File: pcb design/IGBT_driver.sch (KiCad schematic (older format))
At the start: 26 parts, among them Q13 NPN, Q14 PNP, U1 ISO5852S

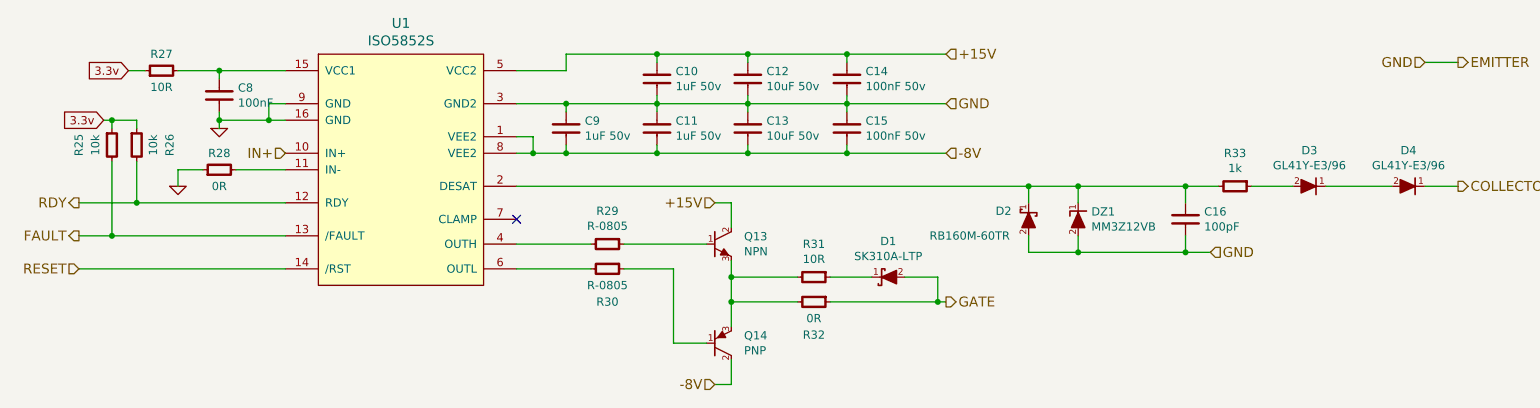
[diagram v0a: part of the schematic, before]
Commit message: Add footprints, more layout and graphics
Signed-off-by: Marcos Chaparro <mchaparro@paltatech.com>
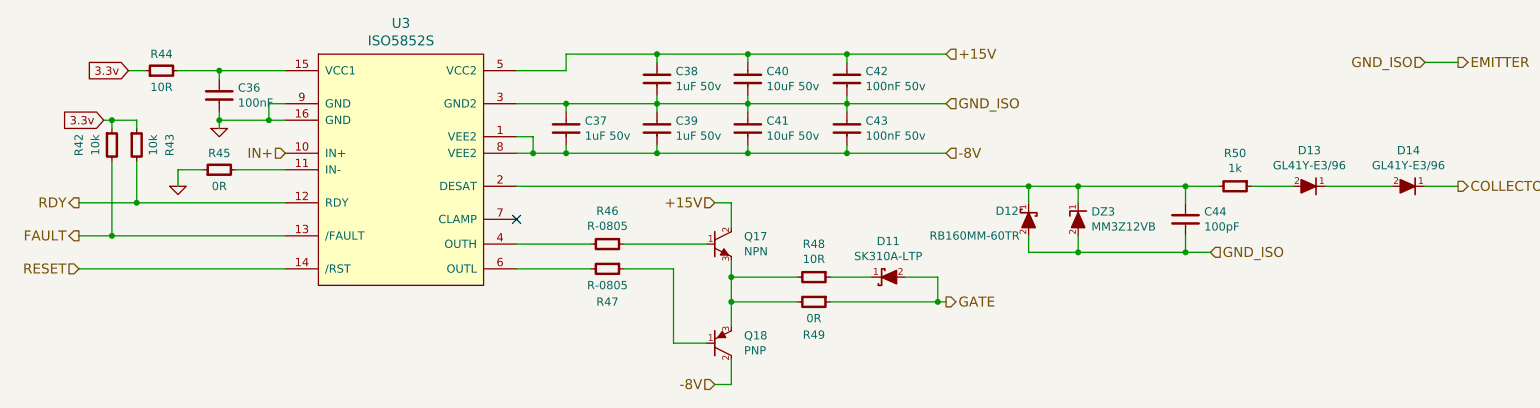
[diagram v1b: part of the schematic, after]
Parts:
- D1: footprint (none) -> w_smd_diode:do214ac
- D2: value RB160M-60TR -> RB160MM-60TR; footprint (none) -> paltatech:SOD-123F; mfg# RB160M-60TR -> RB160MM-60TR
- D3, D4: footprint (none) -> paltatech:melf-DO-213AB
- DZ1: footprint (none) -> smd-semi:SOD-323F
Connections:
- net GND: no longer C10.2, C11.1, C12.2, C13.1, C14.2, C15.1, C16.2, C9.1, D2.2 (A), DZ1.2 (A), U1.3 (GND2)
- new net EMITTER: C10.2, C11.1, C12.2, C13.1, C14.2, C15.1, C16.2, C9.1, D2.2 (A), DZ1.2 (A), U1.3 (GND2)
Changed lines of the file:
@@
 $Descr A4 11693 8268
 encoding utf-8
-Sheet 2 4
+Sheet 4 4
 Title ""
-Date ""
-Rev ""
-Comp ""
+Date "2016-11-09"
+Rev "A"
+Comp "PALTA TECH"
 Comment1 ""
 Comment2 ""
@@
 AR Path="/5822D62D/5822D80D" Ref="U1"  Part="1"
 AR Path="/5824556D/5822D80D" Ref="U3"  Part="1"
-F 0 "U1" H 3750 4837 60  0000 C CNN
+F 0 "U3" H 3750 4837 60  0000 C CNN
 F 1 "ISO5852S" H 3750 4731 60  0000 C CNN
 F 2 "Housings_SOIC:SOIC-16_7.5x10.3mm_Pitch1.27mm" H 3750 3850 60  0001 C CNN
@@
 AR Path="/5822D62D/5822D8A3" Ref="Q13"  Part="1"
 AR Path="/5824556D/5822D8A3" Ref="Q17"  Part="1"
-F 0 "Q13" H 5827 4446 50  0000 L CNN
+F 0 "Q17" H 5827 4446 50  0000 L CNN
 F 1 "NPN" H 5827 4355 50  0000 L CNN
 F 2 "SMD_Packages:DPAK-2" H 5700 4400 60  0001 C CNN
@@
 AR Path="/5822D62D/5822D994" Ref="Q14"  Part="1"
 AR Path="/5824556D/5822D994" Ref="Q18"  Part="1"
-F 0 "Q14" H 5827 5046 50  0000 L CNN
+F 0 "Q18" H 5827 5046 50  0000 L CNN
 F 1 "PNP" H 5827 4955 50  0000 L CNN
 F 2 "SMD_Packages:DPAK-2" H 5700 5000 60  0001 C CNN
@@
 AR Path="/5822D62D/5822DA10" Ref="D1"  Part="1"
 AR Path="/5824556D/5822DA10" Ref="D11"  Part="1"
-F 0 "D1" V 6483 4600 50  0000 C CNN
+F 0 "D11" V 6483 4600 50  0000 C CNN
 F 1 "SK310A-LTP" V 6574 4600 50  0000 C CNN
-F 2 "" H 6700 4600 60  0000 C CNN
+F 2 "w_smd_diode:do214ac" H 6700 4600 60  0001 C CNN
 F 3 "" H 6700 4600 60  0000 C CNN
 F 4 "SK310A-LTP" H 6700 4600 60  0001 C CNN "mfg#"
@@
 AR Path="/5822D62D/5822DB82" Ref="D2"  Part="1"
 AR Path="/5824556D/5822DB82" Ref="D12"  Part="1"
-F 0 "D2" H 7750 4200 50  0000 R CNN
-F 1 "RB160M-60TR" H 8150 4350 50  0000 R CNN
-F 2 "" H 7550 4250 60  0000 C CNN
+F 0 "D12" H 7750 4200 50  0000 R CNN
+F 1 "RB160MM-60TR" H 8150 4350 50  0000 R CNN
+F 2 "paltatech:SOD-123F" H 7550 4250 60  0001 C CNN
 F 3 "" H 7550 4250 60  0000 C CNN
-F 4 "RB160M-60TR" H 7550 4250 60  0001 C CNN "mfg#"
+F 4 "RB160MM-60TR" H 7550 4250 60  0001 C CNN "mfg#"
 	1    7550 4250
 	-1   0    0    1
@@
 AR Path="/5822D62D/5822DBF0" Ref="DZ1"  Part="1"
 AR Path="/5824556D/5822DBF0" Ref="DZ3"  Part="1"
-F 0 "DZ1" H 7930 4296 50  0000 L CNN
+F 0 "DZ3" H 7930 4296 50  0000 L CNN
 F 1 "MM3Z12VB" H 7930 4205 50  0000 L CNN
-F 2 "" H 7850 4250 60  0000 C CNN
+F 2 "smd-semi:SOD-323F" H 7850 4250 60  0001 C CNN
 F 3 "" H 7850 4250 60  0000 C CNN
 F 4 "MM3Z12VB" H 7850 4250 60  0001 C CNN "mfg#"
@@
 AR Path="/5822D62D/5822DD15" Ref="D3"  Part="1"
 AR Path="/5824556D/5822DD15" Ref="D13"  Part="1"
-F 0 "D3" V 9467 4050 50  0000 C CNN
+F 0 "D13" V 9467 4050 50  0000 C CNN
 F 1 "GL41Y-E3/96" V 9376 4050 50  0000 C CNN
-F 2 "" H 9250 4050 60  0000 C CNN
+F 2 "paltatech:melf-DO-213AB" H 9250 4050 60  0001 C CNN
 F 3 "" H 9250 4050 60  0000 C CNN
 F 4 "GL41Y-E3/96" H 9250 4050 60  0001 C CNN "mfg#"
@@
 AR Path="/5822D62D/5822DDF3" Ref="D4"  Part="1"
 AR Path="/5824556D/5822DDF3" Ref="D14"  Part="1"
-F 0 "D4" V 10067 4050 50  0000 C CNN
+F 0 "D14" V 10067 4050 50  0000 C CNN
 F 1 "GL41Y-E3/96" V 9976 4050 50  0000 C CNN
-F 2 "" H 9850 4050 60  0000 C CNN
+F 2 "paltatech:melf-DO-213AB" H 9850 4050 60  0001 C CNN
 F 3 "" H 9850 4050 60  0000 C CNN
 F 4 "GL41Y-E3/96" H 9850 4050 60  0001 C CNN "mfg#"
@@
 AR Path="/5822D62D/58240348" Ref="C10"  Part="1"
 AR Path="/5824556D/58240348" Ref="C38"  Part="1"
-F 0 "C10" H 5413 3446 50  0000 L CNN
+F 0 "C38" H 5413 3446 50  0000 L CNN
 F 1 "1uF 50v" H 5413 3355 50  0000 L CNN
 F 2 "IPC7351-Nominal:CAPC2012X70" H 5300 3400 50  0001 C CNN
@@
 AR Path="/5822D62D/5824044E" Ref="C9"  Part="1"
 AR Path="/5824556D/5824044E" Ref="C37"  Part="1"
-F 0 "C9" H 4863 3746 50  0000 L CNN
+F 0 "C37" H 4863 3746 50  0000 L CNN
 F 1 "1uF 50v" H 4863 3655 50  0000 L CNN
 F 2 "IPC7351-Nominal:CAPC2012X70" H 4750 3700 50  0001 C CNN
@@
 AR Path="/5822D62D/58240493" Ref="C11"  Part="1"
 AR Path="/5824556D/58240493" Ref="C39"  Part="1"
-F 0 "C11" H 5413 3746 50  0000 L CNN
+F 0 "C39" H 5413 3746 50  0000 L CNN
 F 1 "1uF 50v" H 5413 3655 50  0000 L CNN
 F 2 "IPC7351-Nominal:CAPC2012X70" H 5300 3700 50  0001 C CNN
@@
 AR Path="/5822D62D/582406D3" Ref="C12"  Part="1"
 AR Path="/5824556D/582406D3" Ref="C40"  Part="1"
-F 0 "C12" H 5963 3446 50  0000 L CNN
+F 0 "C40" H 5963 3446 50  0000 L CNN
 F 1 "10uF 50v" H 5963 3355 50  0000 L CNN
 F 2 "IPC7351-Nominal:CAPC3216X70" H 5850 3400 50  0001 C CNN
@@
 AR Path="/5822D62D/58240848" Ref="C13"  Part="1"
 AR Path="/5824556D/58240848" Ref="C41"  Part="1"
-F 0 "C13" H 5963 3746 50  0000 L CNN
+F 0 "C41" H 5963 3746 50  0000 L CNN
 F 1 "10uF 50v" H 5963 3655 50  0000 L CNN
 F 2 "IPC7351-Nominal:CAPC3216X70" H 5850 3700 50  0001 C CNN
@@
 AR Path="/5822D62D/582408B6" Ref="C14"  Part="1"
 AR Path="/5824556D/582408B6" Ref="C42"  Part="1"
-F 0 "C14" H 6563 3446 50  0000 L CNN
+F 0 "C42" H 6563 3446 50  0000 L CNN
 F 1 "100nF 50v" H 6563 3355 50  0000 L CNN
 F 2 "IPC7351-Nominal:CAPC2012X70" H 6450 3400 50  0001 C CNN
@@
 AR Path="/5822D62D/58240925" Ref="C15"  Part="1"
 AR Path="/5824556D/58240925" Ref="C43"  Part="1"
-F 0 "C15" H 6563 3746 50  0000 L CNN
+F 0 "C43" H 6563 3746 50  0000 L CNN
 F 1 "100nF 50v" H 6563 3655 50  0000 L CNN
 F 2 "IPC7351-Nominal:CAPC2012X70" H 6450 3700 50  0001 C CNN
@@
 Connection ~ 5850 3850
 Text HLabel 7050 3550 2    60   Input ~ 0
-GND
+GND_ISO
 Text HLabel 7050 3250 2    60   Input ~ 0
 +15V
@@
 AR Path="/5822D62D/5824153A" Ref="R28"  Part="1"
 AR Path="/5824556D/5824153A" Ref="R45"  Part="1"
-F 0 "R28" V 2750 3950 50  0000 C CNN
+F 0 "R45" V 2750 3950 50  0000 C CNN
 F 1 "0R" V 2550 3950 50  0000 C CNN
 F 2 "IPC7351-Nominal:RESC1608X50" H 2650 3950 50  0001 C CNN
@@
 P 2400 4050
 AR Path="/5822D62D/582416B6" Ref="#PWR01"  Part="1"
-AR Path="/5824556D/582416B6" Ref="#PWR015"  Part="1"
-F 0 "#PWR015" H 2400 4050 30  0001 C CNN
+AR Path="/5824556D/582416B6" Ref="#PWR014"  Part="1"
+F 0 "#PWR014" H 2400 4050 30  0001 C CNN
 F 1 "GND" H 2400 3980 30  0001 C CNN
 F 2 "" H 2400 4050 60  0000 C CNN
@@
 P 2650 3700
 AR Path="/5822D62D/58241AEC" Ref="#PWR02"  Part="1"
-AR Path="/5824556D/58241AEC" Ref="#PWR016"  Part="1"
-F 0 "#PWR016" H 2650 3700 30  0001 C CNN
+AR Path="/5824556D/58241AEC" Ref="#PWR015"  Part="1"
+F 0 "#PWR015" H 2650 3700 30  0001 C CNN
 F 1 "GND" H 2650 3630 30  0001 C CNN
 F 2 "" H 2650 3700 60  0000 C CNN
@@
 AR Path="/5822D62D/582417BD" Ref="C8"  Part="1"
 AR Path="/5824556D/582417BD" Ref="C36"  Part="1"
-F 0 "C8" H 2763 3546 50  0000 L CNN
+F 0 "C36" H 2763 3546 50  0000 L CNN
 F 1 "100nF" H 2763 3455 50  0000 L CNN
 F 2 "IPC7351-Nominal:CAPC1608X55" H 2650 3500 50  0001 C CNN
@@
 AR Path="/5822D62D/58241F2C" Ref="R27"  Part="1"
 AR Path="/5824556D/58241F2C" Ref="R44"  Part="1"
-F 0 "R27" V 2400 3350 50  0000 C CNN
+F 0 "R44" V 2400 3350 50  0000 C CNN
 F 1 "10R" V 2200 3350 50  0000 C CNN
 F 2 "IPC7351-Nominal:RESC1608X50" H 2300 3350 50  0001 C CNN
@@
 AR Path="/5822D62D/58242366" Ref="R29"  Part="1"
 AR Path="/5824556D/58242366" Ref="R46"  Part="1"
-F 0 "R29" V 4800 4400 50  0000 C CNN
+F 0 "R46" V 4800 4400 50  0000 C CNN
 F 1 "R-0805" V 4891 4400 50  0000 C CNN
 F 2 "IPC7351-Nominal:RESC2012X50" H 5000 4400 50  0001 C CNN
@@
 AR Path="/5822D62D/5824246D" Ref="R30"  Part="1"
 AR Path="/5824556D/5824246D" Ref="R47"  Part="1"
-F 0 "R30" V 5200 4550 50  0000 C CNN
+F 0 "R47" V 5200 4550 50  0000 C CNN
 F 1 "R-0805" V 5100 4550 50  0000 C CNN
 F 2 "IPC7351-Nominal:RESC2012X50" H 5000 4550 50  0001 C CNN
@@
 AR Path="/5822D62D/5824286A" Ref="R31"  Part="1"
 AR Path="/5824556D/5824286A" Ref="R48"  Part="1"
-F 0 "R31" V 6050 4600 50  0000 C CNN
+F 0 "R48" V 6050 4600 50  0000 C CNN
 F 1 "10R" V 6141 4600 50  0000 C CNN
 F 2 "IPC7351-Nominal:RESC2012X50" H 6250 4600 50  0001 C CNN
@@
 AR Path="/5822D62D/58242871" Ref="R32"  Part="1"
 AR Path="/5824556D/58242871" Ref="R49"  Part="1"
-F 0 "R32" V 6450 4750 50  0000 C CNN
+F 0 "R49" V 6450 4750 50  0000 C CNN
 F 1 "0R" V 6350 4750 50  0000 C CNN
 F 2 "IPC7351-Nominal:RESC2012X50" H 6250 4750 50  0001 C CNN
@@
 AR Path="/5822D62D/58237039" Ref="R25"  Part="1"
 AR Path="/5824556D/58237039" Ref="R42"  Part="1"
-F 0 "R25" V 1800 3800 50  0000 C CNN
+F 0 "R42" V 1800 3800 50  0000 C CNN
 F 1 "10k" V 1900 3800 50  0000 C CNN
 F 2 "IPC7351-Nominal:RESC1608X50" H 2000 3800 50  0001 C CNN
@@
 AR Path="/5822D62D/582375EC" Ref="R26"  Part="1"
 AR Path="/5824556D/582375EC" Ref="R43"  Part="1"
-F 0 "R26" V 2350 3800 50  0000 C CNN
+F 0 "R43" V 2350 3800 50  0000 C CNN
 F 1 "10k" V 2250 3800 50  0000 C CNN
 F 2 "IPC7351-Nominal:RESC1608X50" H 2150 3800 50  0001 C CNN
@@
 AR Path="/5822D62D/5823827A" Ref="C16"  Part="1"
 AR Path="/5824556D/5823827A" Ref="C44"  Part="1"
-F 0 "C16" H 8613 4296 50  0000 L CNN
+F 0 "C44" H 8613 4296 50  0000 L CNN
 F 1 "100pF" H 8613 4205 50  0000 L CNN
 F 2 "IPC7351-Nominal:CAPC2012X70" H 8500 4250 50  0001 C CNN
@@
 AR Path="/5822D62D/582385C6" Ref="R33"  Part="1"
 AR Path="/5824556D/582385C6" Ref="R50"  Part="1"
-F 0 "R33" V 8600 4050 50  0000 C CNN
+F 0 "R50" V 8600 4050 50  0000 C CNN
 F 1 "1k" V 8691 4050 50  0000 C CNN
 F 2 "IPC7351-Nominal:RESC2012X50" H 8800 4050 50  0001 C CNN
@@
 Connection ~ 7850 4450
 Connection ~ 8500 4450
-Text HLabel 8650 4450 2    60   Input ~ 0
-GND
 Text HLabel 10150 4050 2    60   Output ~ 0
 COLLECTOR
@@
 Text HLabel 10150 3300 2    60   Output ~ 0
 EMITTER
-Text HLabel 9950 3300 0    60   Input ~ 0
-GND
 Wire Wire Line
 	9950 3300 10150 3300
@@
 Wire Wire Line
 	1800 4550 3050 4550
+Text HLabel 8650 4450 2    60   Input ~ 0
+GND_ISO
+Text HLabel 9950 3300 0    60   Input ~ 0
+GND_ISO
 $EndSCHEMATC

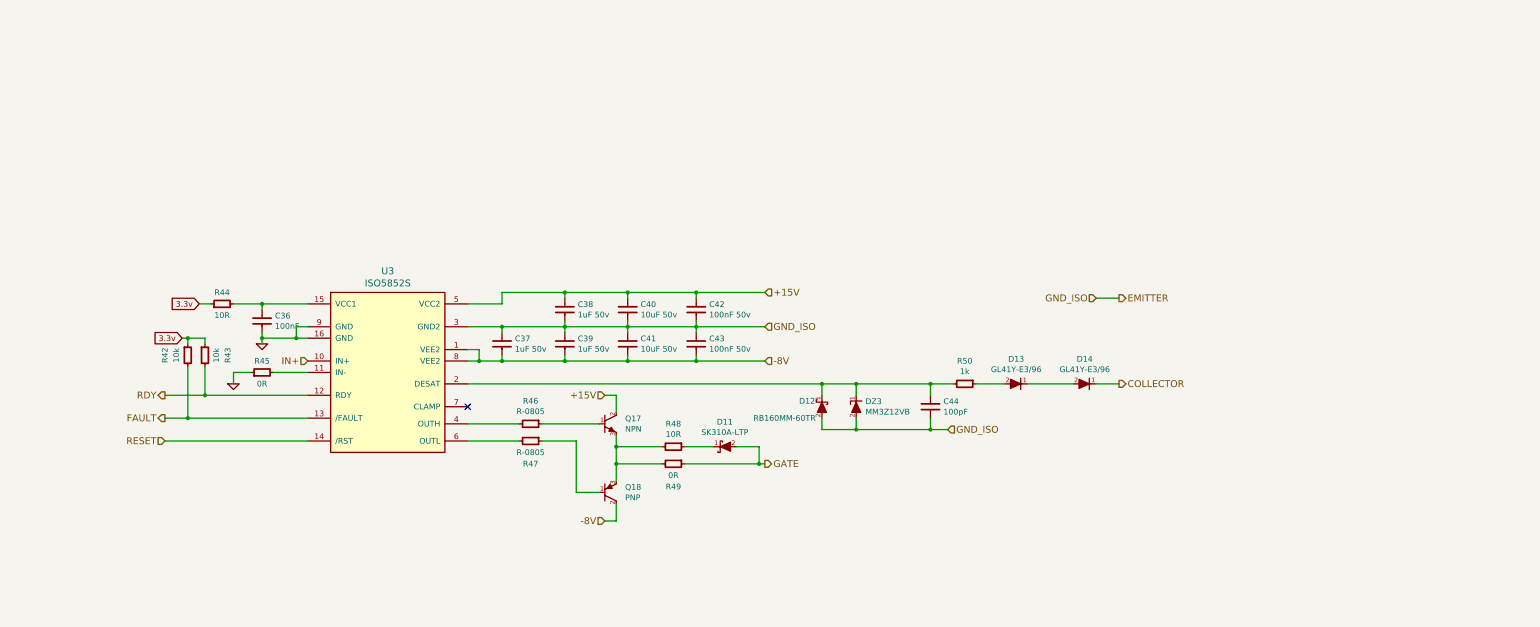
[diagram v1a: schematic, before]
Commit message: Larger gate resistors, added gate caps, added comments and images to the schematic
Signed-off-by: Marcos Chaparro <mchaparro@paltatech.com>
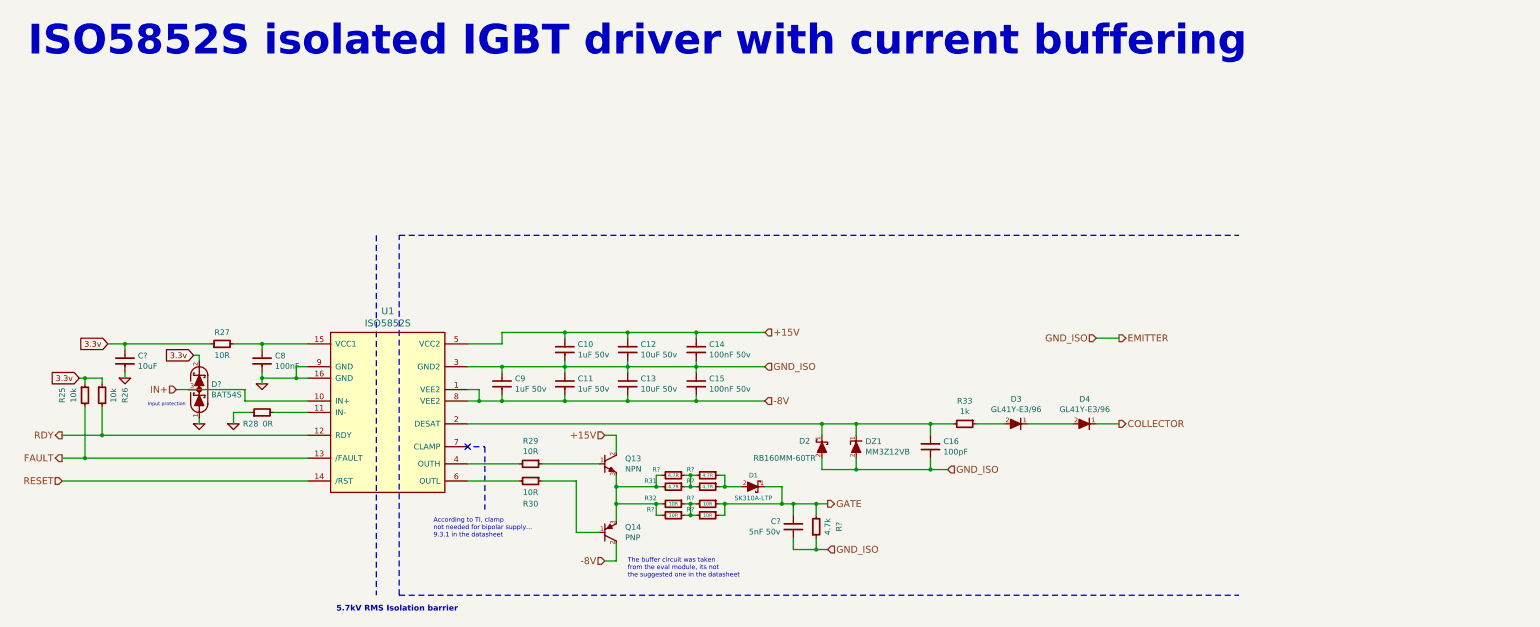
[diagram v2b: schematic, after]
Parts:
- added C?: 5nF 50v, IPC7351-Nominal:CAPC2012X70, symbol C-0805
- added C?: 10uF, IPC7351-Nominal:CAPC1608X55, symbol C-0603
- added D?: BAT54S, smd-semi:SOT-23, symbol BAT54S
- added R?: 4.7k, IPC7351-Nominal:RESC2012X50, symbol R-0805
- added R? (x3): 4.7R, IPC7351-Nominal:RESC3225X60, symbol R-0805
- added R? (x3): 10R, IPC7351-Nominal:RESC3225X60, symbol R-0805
- R29, R30: value R-0805 -> 10R
- R31: value 10R -> 4.7R; footprint IPC7351-Nominal:RESC2012X50 -> IPC7351-Nominal:RESC3225X60; BOM RES SMD 1k 5% [0805] -> RES SMD 1k 5% [2512]
- R32: value 0R -> 10R; footprint IPC7351-Nominal:RESC2012X50 -> IPC7351-Nominal:RESC3225X60; BOM RES SMD 1k 5% [0805] -> RES SMD 1k 5% [2512]
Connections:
- net 3.3v: now also C?.1, D?.2 (K)
- net EMITTER: now also C?.2, R?.1
- net GATE: now also D1.1 (K), C?.1, R?.1, R?.1, R?.2; no longer D1.2 (A), R32.1
- net GND: now also C?.2, D?.1 (A)
- net at Q13.3 (E), Q14.3 (E), R31.2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: now also R?.2, R?.2
- net at R31.1: now also R?.1, R?.2, R?.2; no longer D1.1 (K)
- new net: D1.2 (A), R?.1, R?.1
- new net: R32.1, R?.1, R?.2, R?.2
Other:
- note added: "5.7kV RMS Isolation barrier"
- note added: "According to TI, clamp\nnot needed for bipolar supply...\n9.3.1 in the datasheet"
- note added: "ISO5852S isolated IGBT driver with current buffering"
- note added: "Input protection"
- note added: "The buffer circuit was taken\nfrom the eval module, its not\nthe suggested one in the datasheet"
- moved on the sheet: C10, C11, C12, C13, C14, C15, C16, C8, C9, D1, D2, D3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

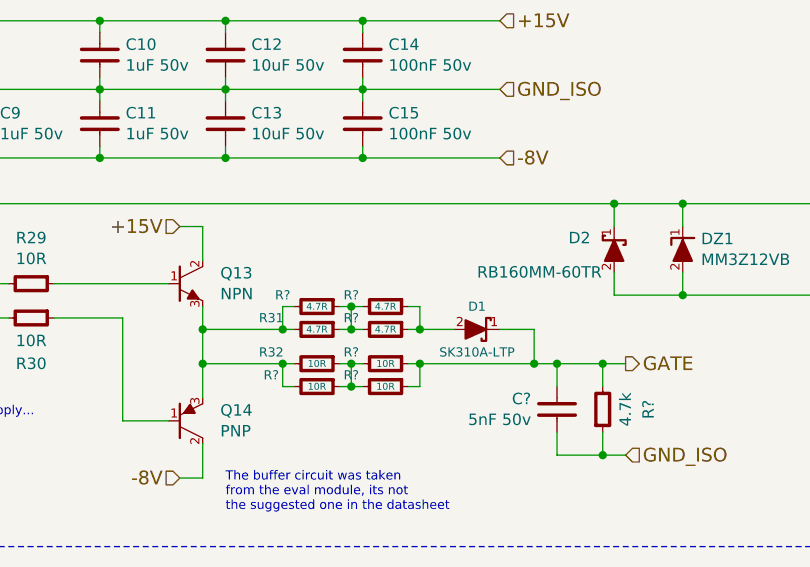
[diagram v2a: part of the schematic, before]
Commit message: Added schottky between gate and 15v supply
Signed-off-by: Marcos Chaparro <mchaparro@paltatech.com>
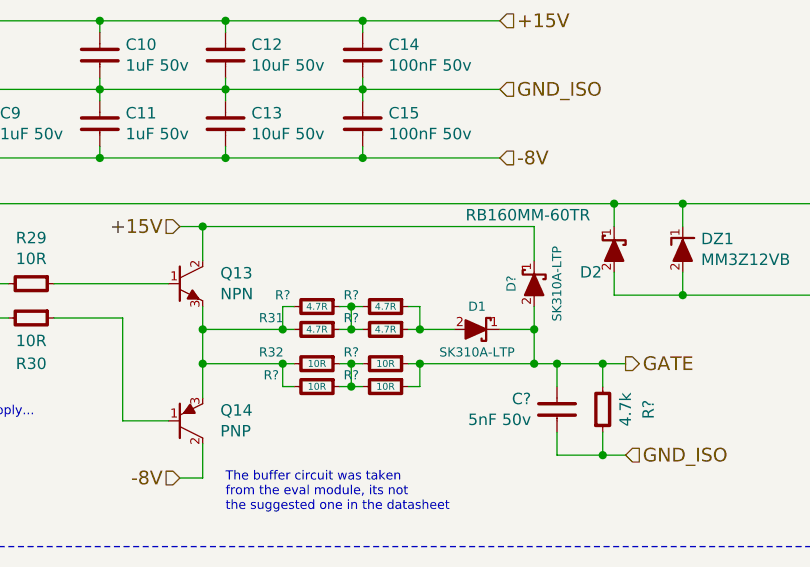
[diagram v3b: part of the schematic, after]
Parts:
- added D?: SK310A-LTP, w_smd_diode:do214ac, symbol SCHOTTKY
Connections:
- net +15V: now also D?.1 (K)
- net GATE: now also D?.2 (A)
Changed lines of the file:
@@
 AR Path="/5822D62D/5822DB82" Ref="D2"  Part="1"
 AR Path="/5824556D/5822DB82" Ref="D12"  Part="1"
-F 0 "D2" H 7750 4550 50  0000 R CNN
-F 1 "RB160MM-60TR" H 8150 4700 50  0000 R CNN
+F 0 "D2" H 7700 4700 50  0000 R CNN
+F 1 "RB160MM-60TR" H 8200 4450 50  0000 R CNN
 F 2 "paltatech:SOD-123F" H 7550 4600 60  0001 C CNN
 F 3 "" H 7550 4600 60  0000 C CNN
@@
 	6650 5100 7600 5100
 Wire Wire Line
-	7200 5100 7200 4950
+	7200 4850 7200 5100
 Wire Wire Line
 	7200 4950 7050 4950
@@
 	5750 4650 5750 4500
 Wire Wire Line
-	5750 4500 5650 4500
+	5650 4500 7200 4500
 Text HLabel 5650 5600 0    60   Input ~ 0
 -8V
@@
 Wire Notes Line
 	4600 4600 4600 5150
+$Comp
+L SCHOTTKY D?
+U 1 1 5833272F
+P 7200 4750
+F 0 "D?" V 7300 4750 40  0000 C CNN
+F 1 "SK310A-LTP" V 7100 4750 40  0000 C CNN
+F 2 "w_smd_diode:do214ac" H 7200 4750 60  0001 C CNN
+F 3 "" H 7200 4750 60  0000 C CNN
+F 4 "SK310A-LTP" H 7200 4750 60  0001 C CNN "mfg#"
+	1    7200 4750
+	-1   0    0    1
+$EndComp
+Connection ~ 7200 4950
+Wire Wire Line
+	7200 4500 7200 4650
+Connection ~ 5750 4500
 $EndSCHEMATC
